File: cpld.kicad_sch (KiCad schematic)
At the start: 0 parts

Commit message: Place CPLD, NCR and last 543 (Latched Trabceiver)
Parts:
- added U6: ATF1508AS-10AU100, 100A_ATM, symbol ATF1508AS:ATF1508AS-10AU100

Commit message: Update design
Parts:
- added J2: Conn_01x06_Pin, symbol Connector:Conn_01x06_Pin
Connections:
- net A5: now reaches U6.10 (I/O)
- net GND: now reaches U6.11 (GND)
- net GND: now also U6.26 (GND), U6.38 (GND), U6.43 (GND), U6.59 (GND), U6.74 (GND), U6.86 (GND), U6.95 (GND)
- net A6: now reaches U6.12 (I/O)
- net A8: now reaches U6.13 (I/O)
- net A17: now reaches U6.14 (I/O)
- net TMS: now reaches U6.15 (I/O/TMS)
- net A18: now reaches U6.16 (I/O)
- net A19: now reaches U6.17 (I/O)
- net V5: now reaches U6.18 (VCCIO)
- net V5: now also U6.3 (VCCIO), U6.34 (VCCIO), U6.51 (VCCIO), U6.66 (VCCIO), U6.82 (VCCIO)
- net A23: now reaches U6.19 (I/O)
- net PLD_DS0: now reaches U6.20 (I/O)
- net PLD_DS1: now reaches U6.21 (I/O)
- net PLD_DS2: now reaches U6.22 (I/O)
- net PLD_DS3: now reaches U6.23 (I/O)
- net PLD_DOE: now reaches U6.24 (I/O)
- net PLD_READ: now reaches U6.27 (I/O)
- net PLD_SCSI: now reaches U6.28 (I/O)
- net PLD_SIZ0: now reaches U6.29 (I/O)
- net PLD_SIZ1: now reaches U6.30 (I/O)
- net PLD_AS: now reaches U6.31 (I/O)
- net PLD_DS: now reaches U6.32 (I/O)
- net PLD_MYBUS: now reaches U6.33 (I/O)
- net STERM: now reaches U6.35 (I/O)
- net SREG: now reaches U6.36 (I/O)
- net IORST: now reaches U6.39 (VCCINT)
- net TDI: now reaches U6.4 (I/O/TDI)
- net NCR_INT: now reaches U6.40 (I/O)
- net PLD_INTVEC: now reaches U6.41 (I/O/PD2)
- net PLD_INTVEC: now also U6.57 (I/O)
- net PLD_FCS: now reaches U6.42 (I/O)
- net Z_SLAVE: now reaches U6.44 (I/O)
- net Z_CFGOUT: now reaches U6.45 (I/O)
- net Z_CFGIN: now reaches U6.46 (I/O)
- net ROM_OE: now reaches U6.47 (I/O)
- net PLD_NACK: now reaches U6.48 (I/O)
- net PLD_INT: now reaches U6.49 (I/O)
- net A0: now reaches U6.5 (I/O)
- net Z_INT2: now reaches U6.50 (I/O)
- net CLK: now reaches U6.52 (I/O)
- net CLKI: now reaches U6.53 (I/O)
- net SLACK: now reaches U6.54 (I/O)
- net PLD_NOZ3: now reaches U6.55 (I/O)
- net PLD_NOZ3: now also U6.90 (INPUT/OE2/GCLK2)
- net PLD_INTREG: now reaches U6.56 (I/O)
- net PLD_MTCR: now reaches U6.58 (I/O)
- net A1: now reaches U6.6 (I/O)
- net MASTER: now reaches U6.60 (I/O)
- net PLD_SID: now reaches U6.61 (I/O)
- net TCK: now reaches U6.62 (I/O/TCK)
- net Z_DTACK: now reaches U6.63 (I/O)
- net D2Z: now reaches U6.64 (I/O)
- net Z2D_TO_FB: now reaches U6.65 (I/O)
- net DBLT: now reaches U6.67 (I/O)
- net DBOE_TO_FB: now reaches U6.68 (I/O)
- net ABOEL: now reaches U6.69 (I/O)
- net A2: now reaches U6.7 (I/O)
- net ABOEH: now reaches U6.70 (I/O)
- net Z_LOCK: now reaches U6.71 (I/O)
- net PLD_INTSPC: now reaches U6.72 (I/O)
- net TDO: now reaches U6.73 (I/O/TDO)
- net PLD_FC2: now reaches U6.75 (I/O)
- net Z_MTACK: now reaches U6.76 (I/O)
- net CBREQ: now reaches U6.77 (I/O)
- net BERR: now reaches U6.78 (I/O)
- net PLD_ASQ: now reaches U6.79 (I/O)
- net A3: now reaches U6.8 (I/O)
- net Z_FCS_TO_FB: now reaches U6.80 (I/O)
- net CBACK: now reaches U6.81 (I/O)
- net PLD_FC1: now reaches U6.83 (I/O)
- net PLD_FC0: now reaches U6.84 (I/O)
- net Z_SENSEZ3: now reaches U6.85 (I/O/GCLK3)
- net PLD_CFGLT: now reaches U6.87 (INPUT/GCLK1)
- net Z_CINH: now reaches U6.88 (INPUT/OE1)
- net MATCH: now reaches U6.89 (INPUT/GCLR)
- net A4: now reaches U6.9 (I/O)
- net Z_BGn: now reaches U6.92 (I/O)
- net Z_BRn: now reaches U6.93 (I/O)
- net BMASTER: now reaches U6.94 (I/O)
- net SBR: now reaches U6.96 (I/O)
- net SBG: now reaches U6.97 (I/O)
- net Z_7M: now reaches U6.98 (I/O)
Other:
- moved on the sheet: U6

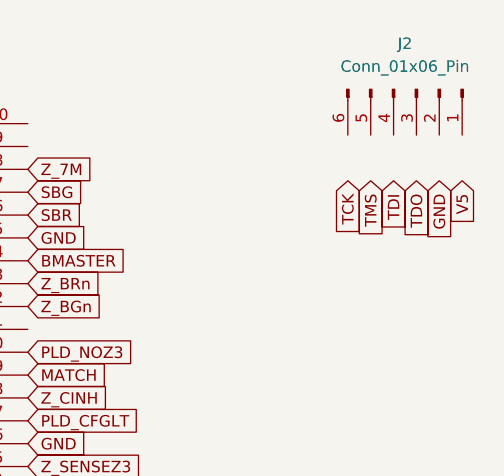
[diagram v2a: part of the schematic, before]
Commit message: Redraw footprints, finish Termination/Connectors
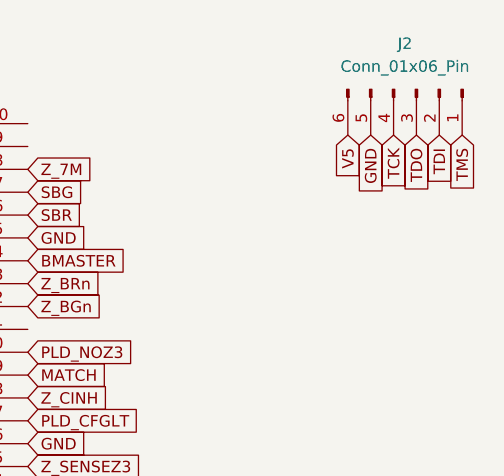
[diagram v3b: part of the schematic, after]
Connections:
- net GND: now also J2.5 (Pin_5)
- net TCK: now also J2.4 (Pin_4)
- net TDI: now also J2.2 (Pin_2)
- net TDO: now also J2.3 (Pin_3)
- net TMS: now also J2.1 (Pin_1)
- net V5: now also J2.6 (Pin_6)
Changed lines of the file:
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@@
 	(global_label "GND"
 		(shape input)
-		(at 168.91 35.56 270)
-		(fields_autoplaced yes)
-		(effects
-			(font
-				(size 1.27 1.27)
-			)
-			(justify right)
-		)
-		(property "Intersheetrefs" "${INTERSHEET_REFS}"
-			(at 168.91 42.4157 90)
+		(at 161.29 30.48 270)
+		(fields_autoplaced yes)
+		(effects
+			(font
+				(size 1.27 1.27)
+			)
+			(justify right)
+		)
+		(property "Intersheetrefs" "${INTERSHEET_REFS}"
+			(at 161.29 37.3357 90)
 			(effects
 				(font
@@
 	(global_label "TDO"
 		(shape input)
-		(at 166.37 35.56 270)
-		(fields_autoplaced yes)
-		(effects
-			(font
-				(size 1.27 1.27)
-			)
-			(justify right)
-		)
-		(property "Intersheetrefs" "${INTERSHEET_REFS}"
-			(at 166.37 42.1133 90)
+		(at 166.37 30.48 270)
+		(fields_autoplaced yes)
+		(effects
+			(font
+				(size 1.27 1.27)
+			)
+			(justify right)
+		)
+		(property "Intersheetrefs" "${INTERSHEET_REFS}"
+			(at 166.37 37.0333 90)
 			(effects
 				(font
@@
 	(global_label "TCK"
 		(shape input)
-		(at 158.75 35.56 270)
-		(fields_autoplaced yes)
-		(effects
-			(font
-				(size 1.27 1.27)
-			)
-			(justify right)
-		)
-		(property "Intersheetrefs" "${INTERSHEET_REFS}"
-			(at 158.75 42.0528 90)
+		(at 163.83 30.48 270)
+		(fields_autoplaced yes)
+		(effects
+			(font
+				(size 1.27 1.27)
+			)
+			(justify right)
+		)
+		(property "Intersheetrefs" "${INTERSHEET_REFS}"
+			(at 163.83 36.9728 90)
 			(effects
 				(font
@@
 	(global_label "TDI"
 		(shape input)
-		(at 163.83 35.56 270)
-		(fields_autoplaced yes)
-		(effects
-			(font
-				(size 1.27 1.27)
-			)
-			(justify right)
-		)
-		(property "Intersheetrefs" "${INTERSHEET_REFS}"
-			(at 163.83 41.3876 90)
+		(at 168.91 30.48 270)
+		(fields_autoplaced yes)
+		(effects
+			(font
+				(size 1.27 1.27)
+			)
+			(justify right)
+		)
+		(property "Intersheetrefs" "${INTERSHEET_REFS}"
+			(at 168.91 36.3076 90)
 			(effects
 				(font
@@
 	(global_label "V5"
 		(shape input)
-		(at 171.45 35.56 270)
-		(fields_autoplaced yes)
-		(effects
-			(font
-				(size 1.27 1.27)
-			)
-			(justify right)
-		)
-		(property "Intersheetrefs" "${INTERSHEET_REFS}"
-			(at 171.45 40.8433 90)
+		(at 158.75 30.48 270)
+		(fields_autoplaced yes)
+		(effects
+			(font
+				(size 1.27 1.27)
+			)
+			(justify right)
+		)
+		(property "Intersheetrefs" "${INTERSHEET_REFS}"
+			(at 158.75 35.7633 90)
 			(effects
 				(font
@@
 	(global_label "TMS"
 		(shape input)
-		(at 161.29 35.56 270)
-		(fields_autoplaced yes)
-		(effects
-			(font
-				(size 1.27 1.27)
-			)
-			(justify right)
-		)
-		(property "Intersheetrefs" "${INTERSHEET_REFS}"
-			(at 161.29 42.1737 90)
-			(effects
-				(font
+		(at 171.45 30.48 270)
+		(fields_autoplaced yes)
+		(effects
+			(font
+				(size 1.27 1.27)
+			)
+			(justify right)
+		)
+		(property "Intersheetrefs" "${INTERSHEET_REFS}"
+			(at 171.45 37.0937 90)
+			(effects
+				(font

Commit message: More work. Getting there.
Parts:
- added C11, C12, C13, C14, C15, C16, C17: 0.1uF, symbol Device:C_Small
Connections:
- net GND: now also C11.2, C12.2, C13.2, C14.2, C15.2, C16.2, C17.2
- net V5: now also C11.1, C12.1, C13.1, C14.1, C15.1, C16.1, C17.1

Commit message: Latest updates
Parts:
- C11, C12, C13, C14, C15, C16, C17: value 0.1uF -> 100nF; footprint (none) -> Capacitor_SMD:C_0603_1608Metric_Pad1.08x0.95mm_HandSolder
- J2: footprint (none) -> Connector_PinHeader_2.54mm:PinHeader_1x06_P2.54mm_Vertical
- U6: footprint 100A_ATM -> ATF1508AS:100A_ATM
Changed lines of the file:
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@@
 			)
 		)
-		(property "Footprint" ""
+		(property "Footprint" "Connector_PinHeader_2.54mm:PinHeader_1x06_P2.54mm_Vertical"
 			(at 166.37 25.4 0)
 			(effects
@@
 			)
 		)
-		(property "Footprint" "100A_ATM"
+		(property "Footprint" "ATF1508AS:100A_ATM"
 			(at 31.75 29.21 0)
 			(effects
@@
 			)
 		)
-		(property "Value" "0.1uF"
+		(property "Value" "100nF"
 			(at 160.02 62.2362 0)
 			(effects
@@
 			)
 		)
-		(property "Footprint" ""
+		(property "Footprint" "Capacitor_SMD:C_0603_1608Metric_Pad1.08x0.95mm_HandSolder"
 			(at 157.48 60.96 0)
 			(effects
@@
 			)
 		)
-		(property "Value" "0.1uF"
+		(property "Value" "100nF"
 			(at 180.34 62.2362 0)
 			(effects
@@
 			)
 		)
-		(property "Footprint" ""
+		(property "Footprint" "Capacitor_SMD:C_0603_1608Metric_Pad1.08x0.95mm_HandSolder"
 			(at 177.8 60.96 0)
 			(effects
@@
 			)
 		)
-		(property "Value" "0.1uF"
+		(property "Value" "100nF"
 			(at 179.07 53.3462 0)
 			(effects
@@
 			)
 		)
-		(property "Footprint" ""
+		(property "Footprint" "Capacitor_SMD:C_0603_1608Metric_Pad1.08x0.95mm_HandSolder"
 			(at 176.53 52.07 0)
 			(effects
@@
 			)
 		)
-		(property "Value" "0.1uF"
+		(property "Value" "100nF"
 			(at 160.02 53.3462 0)
 			(effects
@@
 			)
 		)
-		(property "Footprint" ""
+		(property "Footprint" "Capacitor_SMD:C_0603_1608Metric_Pad1.08x0.95mm_HandSolder"
 			(at 157.48 52.07 0)
 			(effects
@@
 			)
 		)
-		(property "Value" "0.1uF"
+		(property "Value" "100nF"
 			(at 189.23 53.3462 0)
 			(effects
@@
 			)
 		)
-		(property "Footprint" ""
+		(property "Footprint" "Capacitor_SMD:C_0603_1608Metric_Pad1.08x0.95mm_HandSolder"
 			(at 186.69 52.07 0)
 			(effects
@@
 			)
 		)
-		(property "Value" "0.1uF"
+		(property "Value" "100nF"
 			(at 170.18 53.3462 0)
 			(effects
@@
 			)
 		)
-		(property "Footprint" ""
+		(property "Footprint" "Capacitor_SMD:C_0603_1608Metric_Pad1.08x0.95mm_HandSolder"
 			(at 167.64 52.07 0)
 			(effects
@@
 			)
 		)
-		(property "Value" "0.1uF"
+		(property "Value" "100nF"
 			(at 170.18 62.2362 0)
 			(effects
@@
 			)
 		)
-		(property "Footprint" ""
+		(property "Footprint" "Capacitor_SMD:C_0603_1608Metric_Pad1.08x0.95mm_HandSolder"
 			(at 167.64 60.96 0)
 			(effects

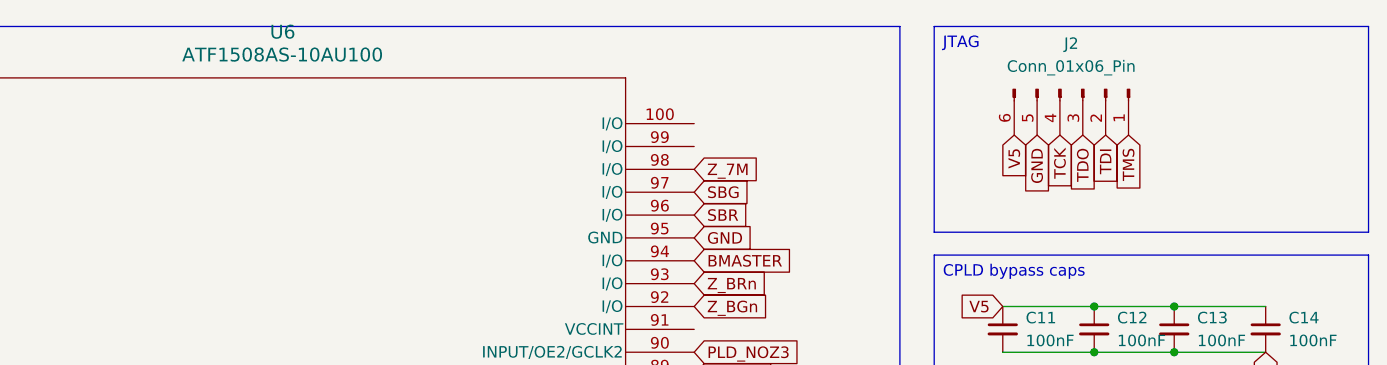
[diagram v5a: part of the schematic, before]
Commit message: Update RN footprint to CAY16_102J4LF
- Rename RNs from R to RN.
- Fix U5 footprint
- Rename pages to be consecutive numbers
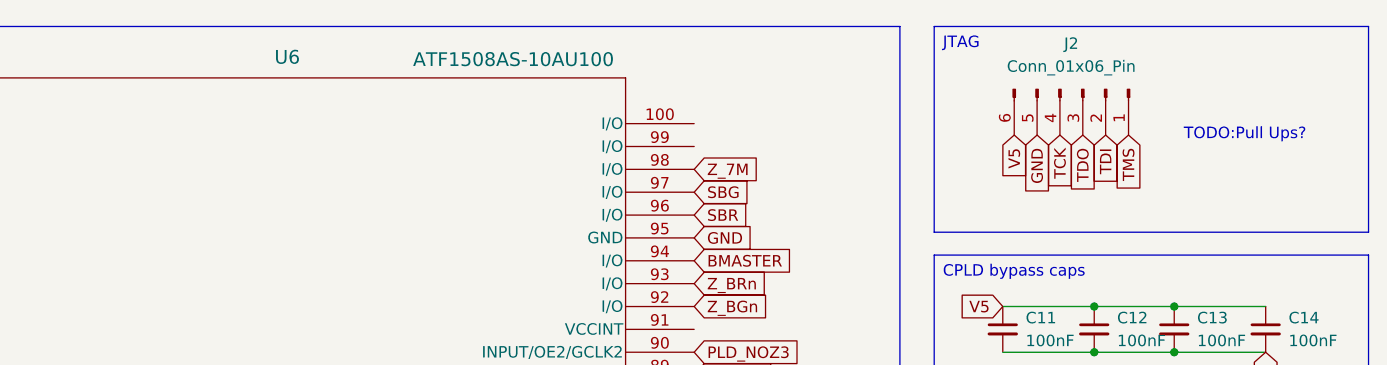
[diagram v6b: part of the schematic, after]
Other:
- note added: "TODO:Pull Ups?"
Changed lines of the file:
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@@
 	(generator_version "9.0")
 	(paper "A4")
+	(text "TODO:Pull Ups?"
+		(exclude_from_sim no)
+		(at 184.404 30.48 0)
+		(effects
+			(font
+				(size 1.27 1.27)
+			)
+		)
+	)
 	(text_box "CPLD - No more GALs"
 		(exclude_from_sim no)
@@
 		(on_board yes)
 		(dnp no)
-		(fields_autoplaced yes)
 		(property "Reference" "U6"
-			(at 77.47 19.05 0)
+			(at 77.978 21.844 0)
 			(effects
 				(font
@@
 		)
 		(property "Value" "ATF1508AS-10AU100"
-			(at 77.47 21.59 0)
-			(effects
-				(font
+			(at 103.124 22.098 0)
+			(effects
+				(font

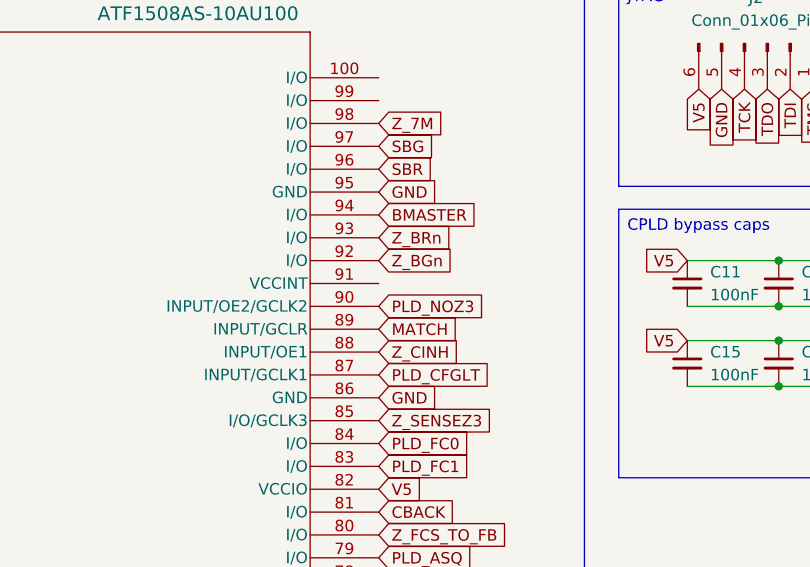
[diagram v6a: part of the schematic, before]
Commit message: Connect VCCINT on CPLD, add GND and V5 to power symbols
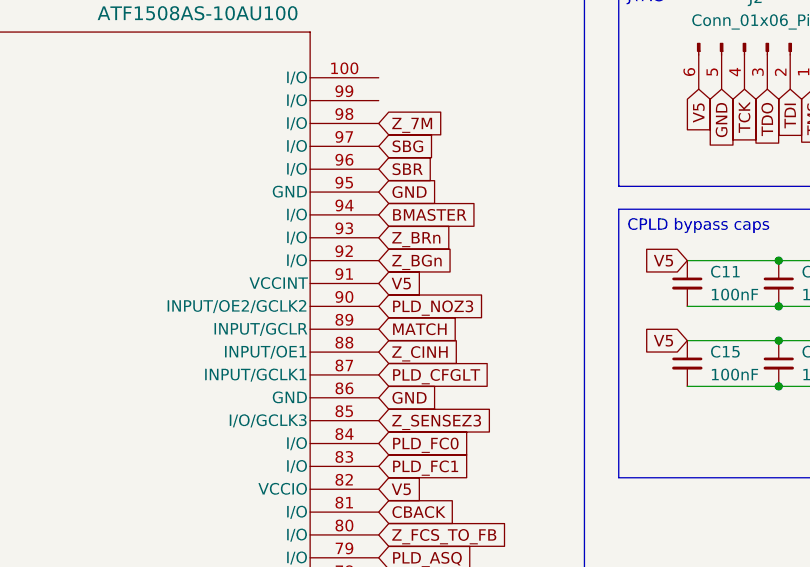
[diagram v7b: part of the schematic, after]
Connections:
- net V5: now also U6.91 (VCCINT)
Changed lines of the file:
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@@
+		)
+	)
+	(global_label "V5"
+		(shape input)
+		(at 123.19 52.07 0)
+		(fields_autoplaced yes)
+		(effects
+			(font
+				(size 1.27 1.27)
+			)
+			(justify left)
+		)
+		(property "Intersheetrefs" "${INTERSHEET_REFS}"
+			(at 128.4733 52.07 0)
+			(effects
+				(font
+					(size 1.27 1.27)
+				)
+				(justify left)
+				(hide yes)
+			)
 		)
 	)
